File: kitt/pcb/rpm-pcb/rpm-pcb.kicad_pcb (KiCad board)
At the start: 2 copper layers, 430 x 139 mm, 178 parts, among them J1 Screw_Terminal_01x02, J2 Screw_Terminal_01x02, Q1 NDP6020P, Q2 NDP6020P, Q3 NDP6020P, Q4 NDP6020P, Q5 NDP6020P, Q6 NDP6020P, U1 TLC5940NT, U2 TLC5940NT, U3 TLC5940NT, U4 TLC5940NT, U5 TLC5940NT, U6 TLC5940NT, U7 TLC5940NT, U8 TLC5940NT, U9 TLC5940NT

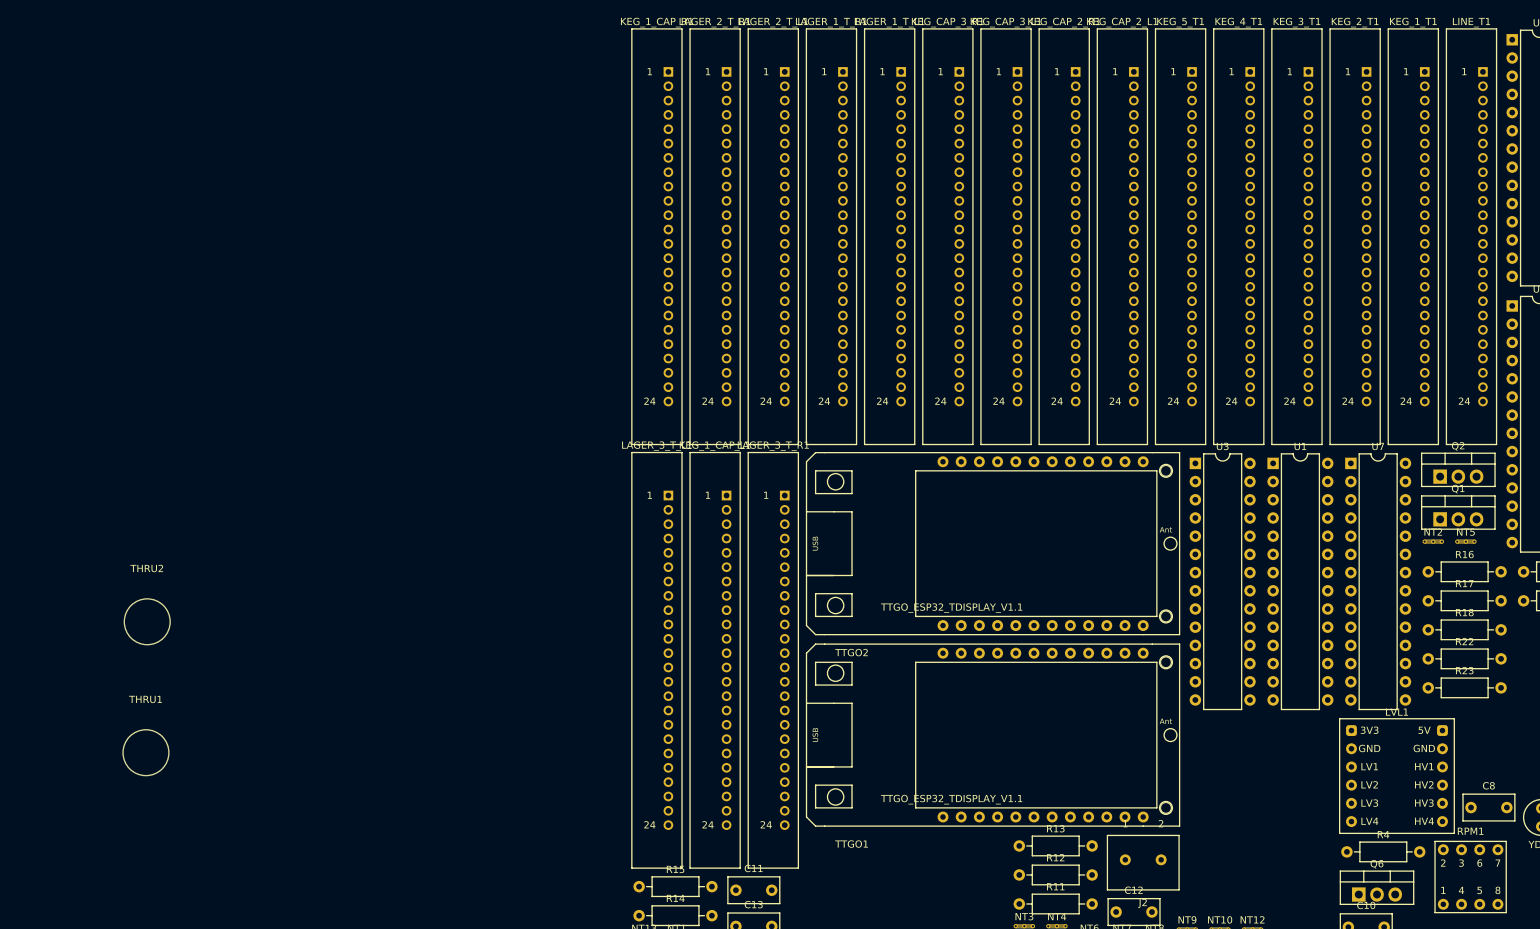
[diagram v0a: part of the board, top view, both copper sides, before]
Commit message: fixed 12 seg leds
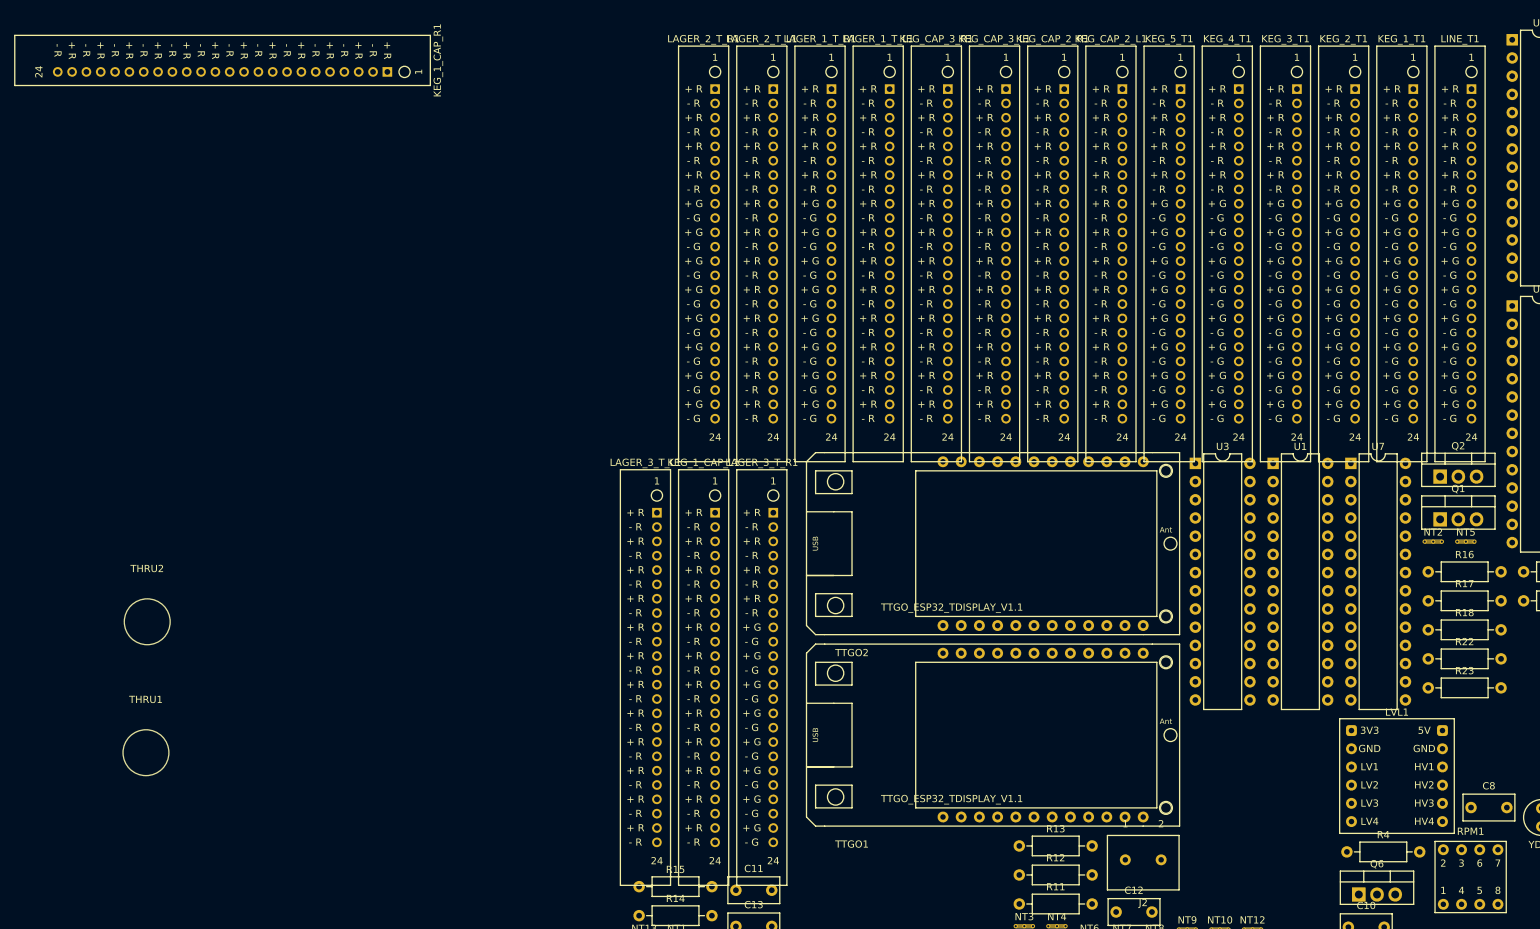
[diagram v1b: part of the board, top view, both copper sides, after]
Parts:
- KEG_1_CAP_L1, KEG_1_CAP_R1, KEG_CAP_2_L1, KEG_CAP_2_R1, KEG_CAP_3_L1, KEG_CAP_3_R1, LAGER_1_T_L1, LAGER_2_T_L1, LAGER_3_T_L1: footprint KITT-Footpads:LED_12_Segment_2.0mm_24_pin -> KITT-Footpads:KYX_125807R
- KEG_1_T1, KEG_2_T1, KEG_3_T1, KEG_4_T1, KEG_5_T1, LAGER_1_T_R1, LAGER_2_T_R1, LAGER_3_T_R1, LINE_T1: footprint KITT-Footpads:LED_12_Segment_2.0mm_24_pin -> KITT-Footpads:STBD001_4R8G
- moved KEG_1_CAP_R1 35.2 mm to (82.2, -68.9), turned to 270 degrees

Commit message: 220 tab down
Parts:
- Q4, Q5, Q6: footprint Package_TO_SOT_THT:TO-220-3_Vertical -> Package_TO_SOT_THT:TO-220-3_Horizontal_TabDown
